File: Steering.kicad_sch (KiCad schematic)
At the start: 63 parts, among them J12 SERVO, J508 Conn_01x13, J509 Conn_01x03, J510 SWD, SW11 219-2MSTR, SW12 219-2MSTR, SW13 CVS-01TB, SW14 CVS-01TB, SW506 SW_Push, U13 STM32F401RETx, U14 MCP2515T-I/ST, U15 MCP2515T-I/ST, U16 SN65HVD230DR, U17 SN65HVD230DR, U18 INA180A1IDBVT, Y5 16 MHz, Y6 16 MHz

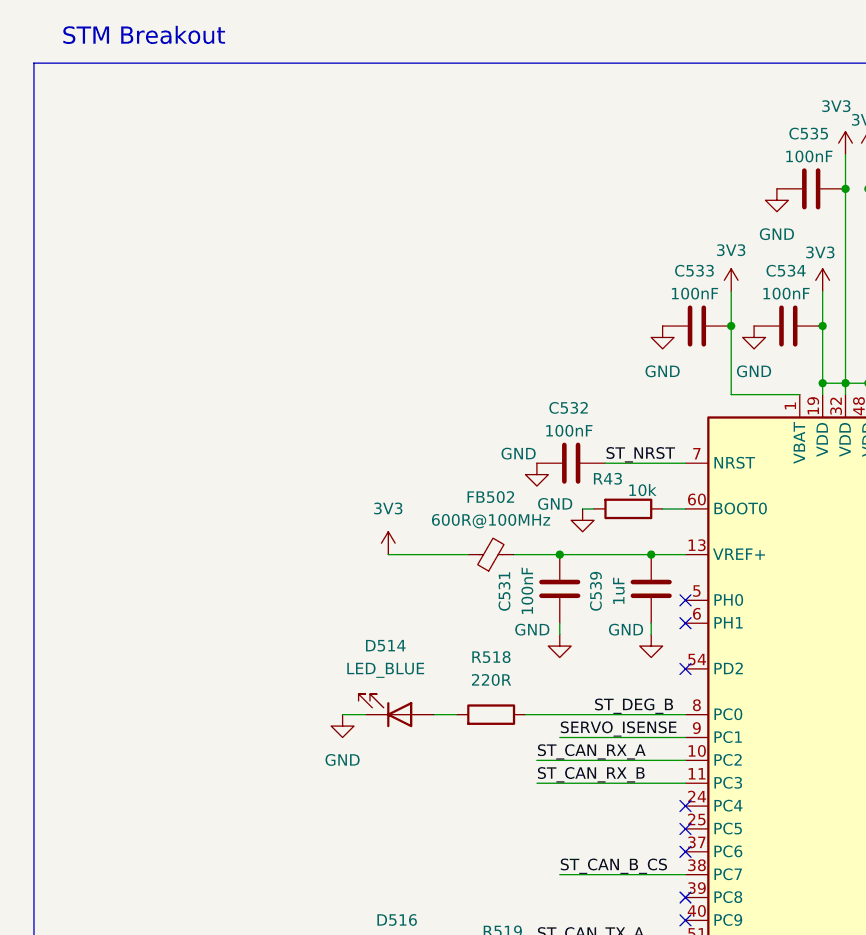
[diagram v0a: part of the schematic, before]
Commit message: Added 16MHz crystals to both STMs
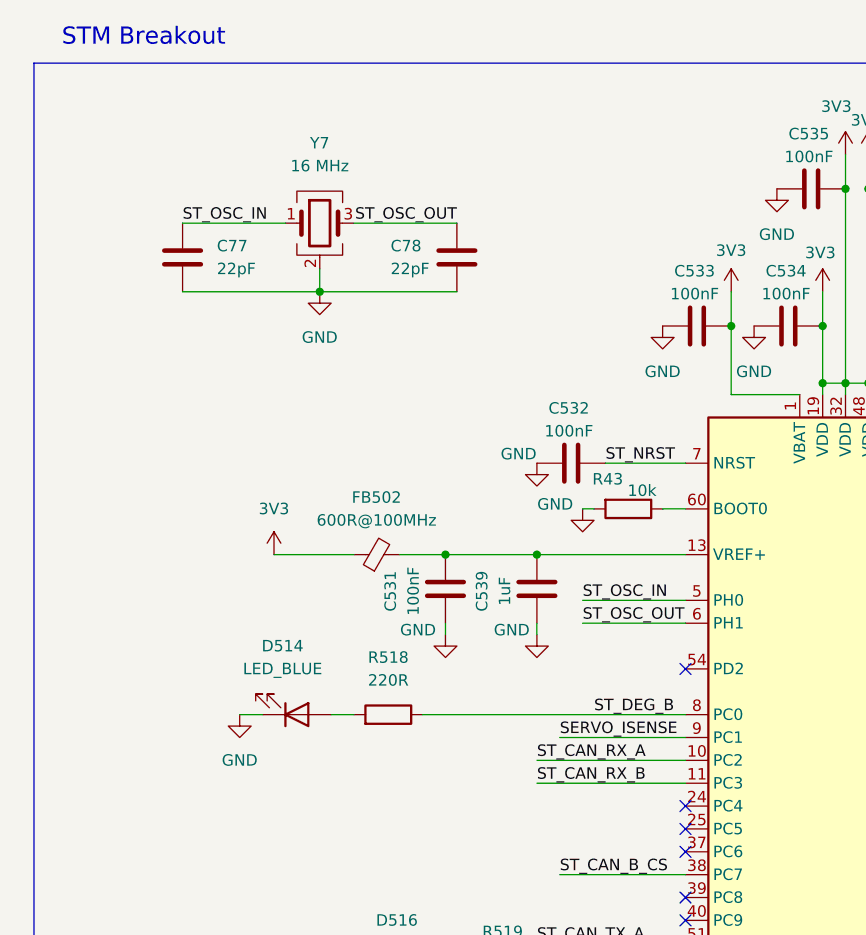
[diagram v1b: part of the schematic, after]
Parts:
- added C77, C78: 22pF, Capacitor_SMD:C_0603_1608Metric, symbol Device:C
- added Y7: 16 MHz, Crystal:Crystal_SMD_3225-4Pin_3.2x2.5mm, symbol Device:Crystal_GND24
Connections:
- net GND: now also C77.2, C78.2, Y7.2 (G), Y7.4 (G)
- net ST_OSC_IN: now reaches U13.5 (PH0)
- net ST_OSC_IN: now also C77.1, Y7.1
- net ST_OSC_OUT: now reaches U13.6 (PH1)
- net ST_OSC_OUT: now also C78.1, Y7.3
- no-connect marks 38 -> 36
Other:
- moved on the sheet: C531, C539, D514, FB502, R518

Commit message: Placement & Routing progress for ST and 8V buck
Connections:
- net SERVO_ISENSE: now also U13.14 (PA0); no longer U13.9 (PC1)
- net SERVO_PWM: now also J508.9 (Pin_9)
- net ST_CAN_RX_A: now also U13.37 (PC6); no longer U13.10 (PC2)
- net ST_CAN_RX_B: now also U13.36 (PB15); no longer U13.11 (PC3)
- net ST_CAN_TX_A: now also U13.35 (PB14); no longer U13.51 (PC10)
- net ST_CAN_TX_B: now also U13.34 (PB13); no longer U13.52 (PC11)
- net ST_DEG_A: now also R518.1, U13.8 (PC0); no longer R521.2, U13.61 (PB8)
- net ST_DEG_B: now also R521.1, U13.9 (PC1); no longer R518.1, U13.8 (PC0)
- net at D515.2 (A): now also R521.2; no longer R521.1
- net SRV: no longer names the net of U13.62 (PB9)
- net SRV: no longer J508.9 (Pin_9)
- no-connect marks 36 -> 37
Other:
- moved on the sheet: D517, R522

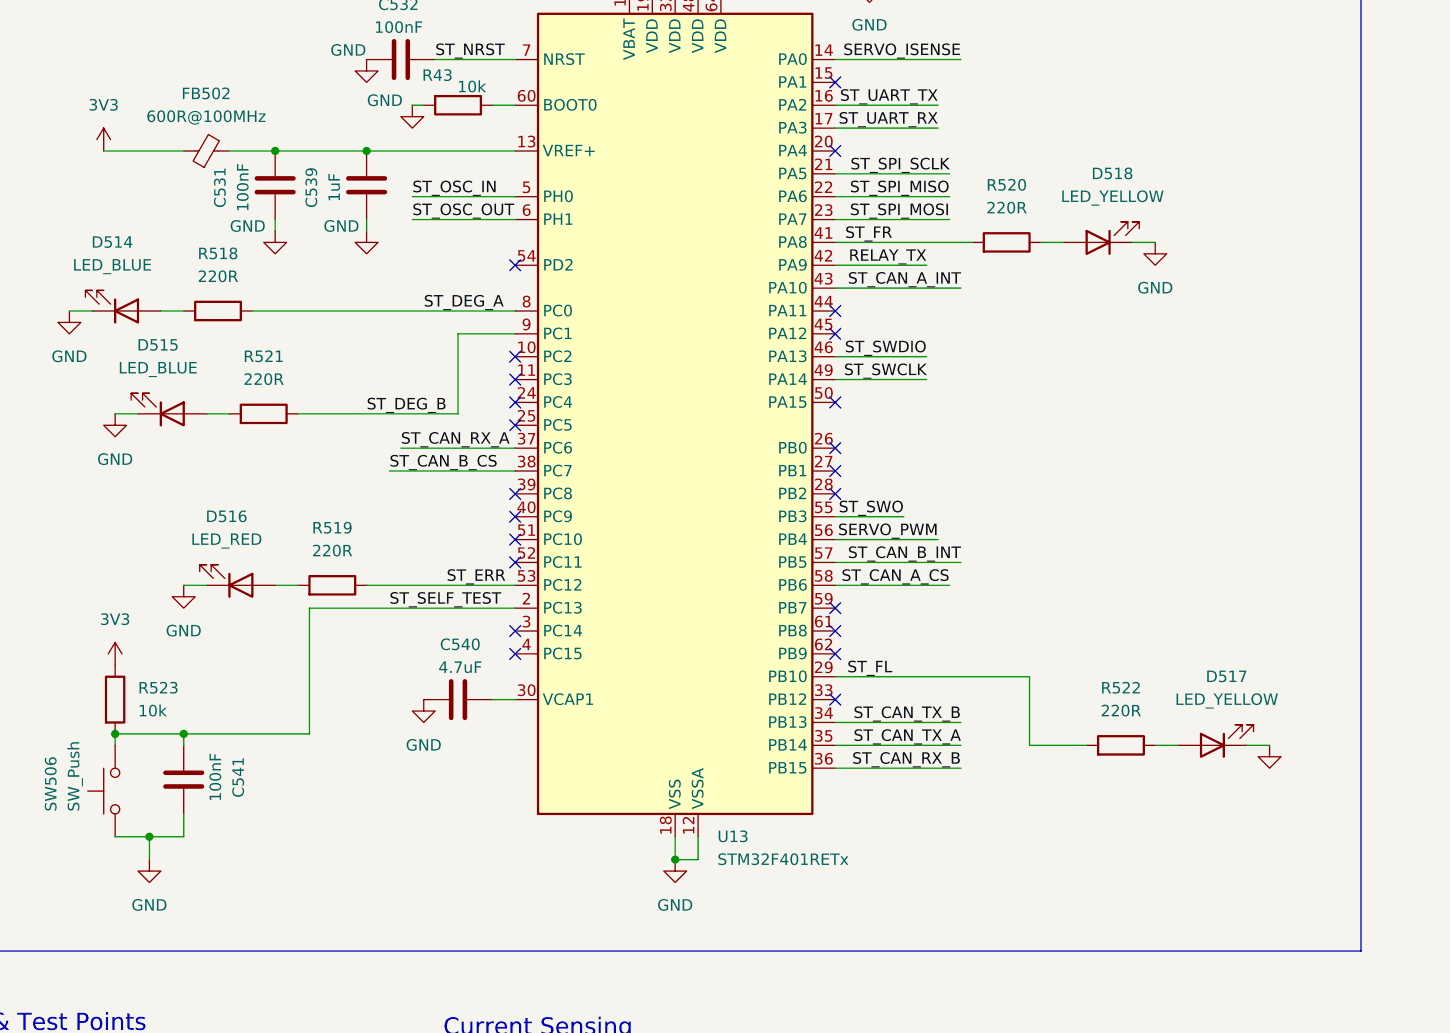
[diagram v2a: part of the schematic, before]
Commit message: Reduced congestion on steering
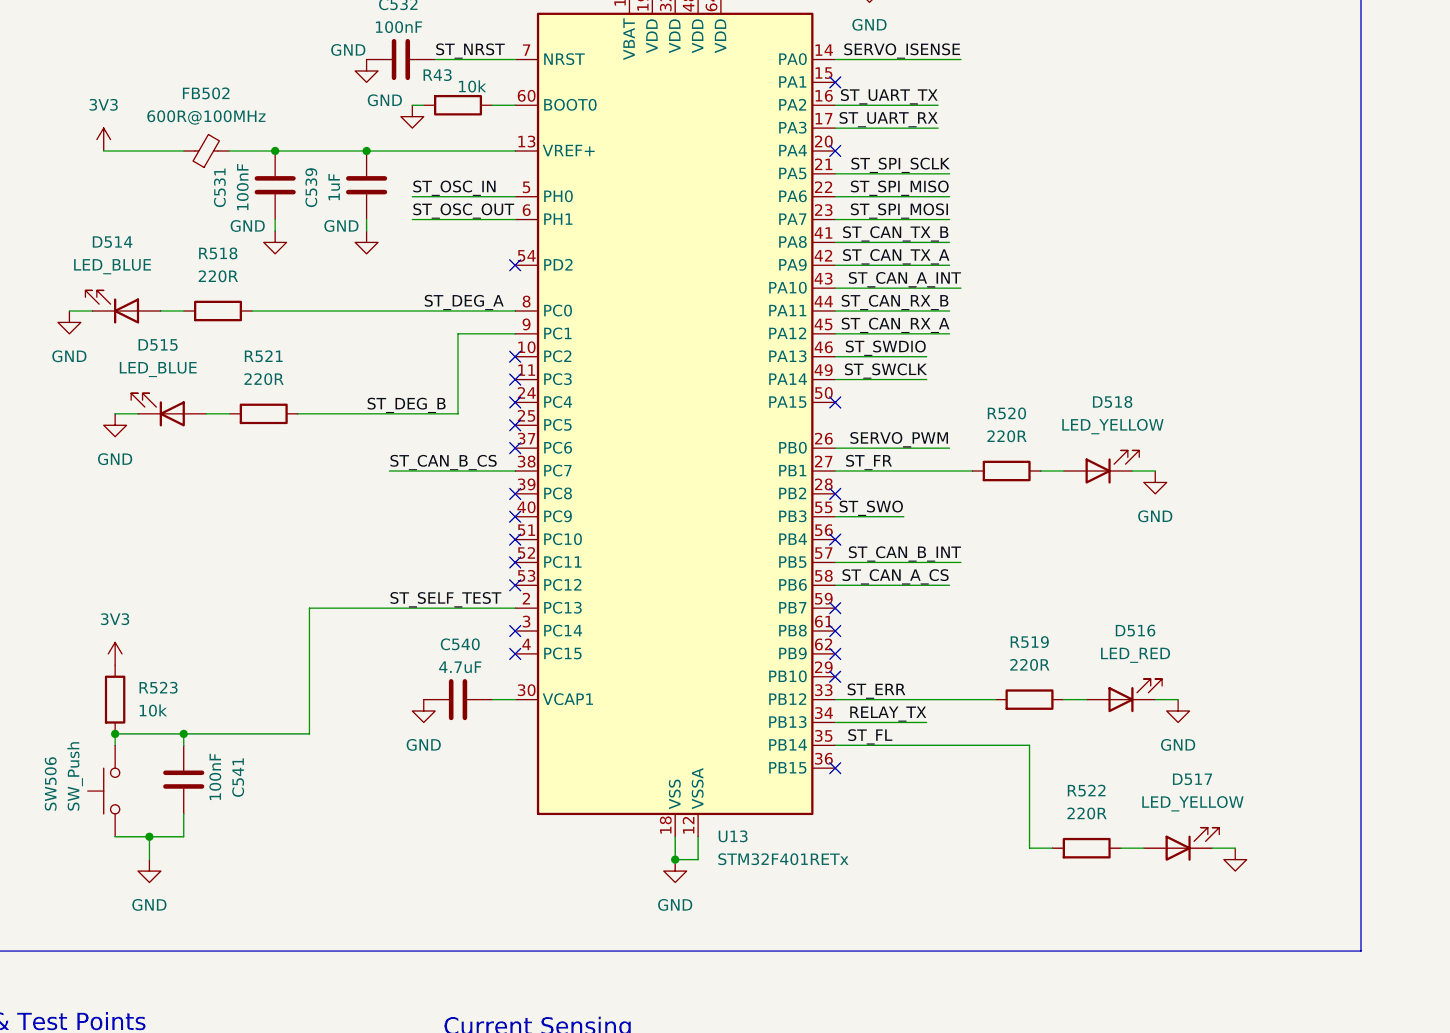
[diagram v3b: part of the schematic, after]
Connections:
- net RELAY_TX: now also U13.34 (PB13); no longer U13.42 (PA9)
- net SERVO_PWM: now also U13.26 (PB0); no longer U13.56 (PB4)
- net ST_CAN_RX_A: now also U13.45 (PA12); no longer U13.37 (PC6)
- net ST_CAN_RX_B: now also U13.44 (PA11); no longer U13.36 (PB15)
- net ST_CAN_TX_A: now also U13.42 (PA9); no longer U13.35 (PB14)
- net ST_CAN_TX_B: now also U13.41 (PA8); no longer U13.34 (PB13)
- net ST_ERR: now also R519.2, U13.33 (PB12); no longer R519.1, U13.53 (PC12)
- net ST_FL: now also U13.35 (PB14); no longer U13.29 (PB10)
- net ST_FR: now also U13.27 (PB1); no longer U13.41 (PA8)
- net at D516.2 (A): now also R519.1; no longer R519.2

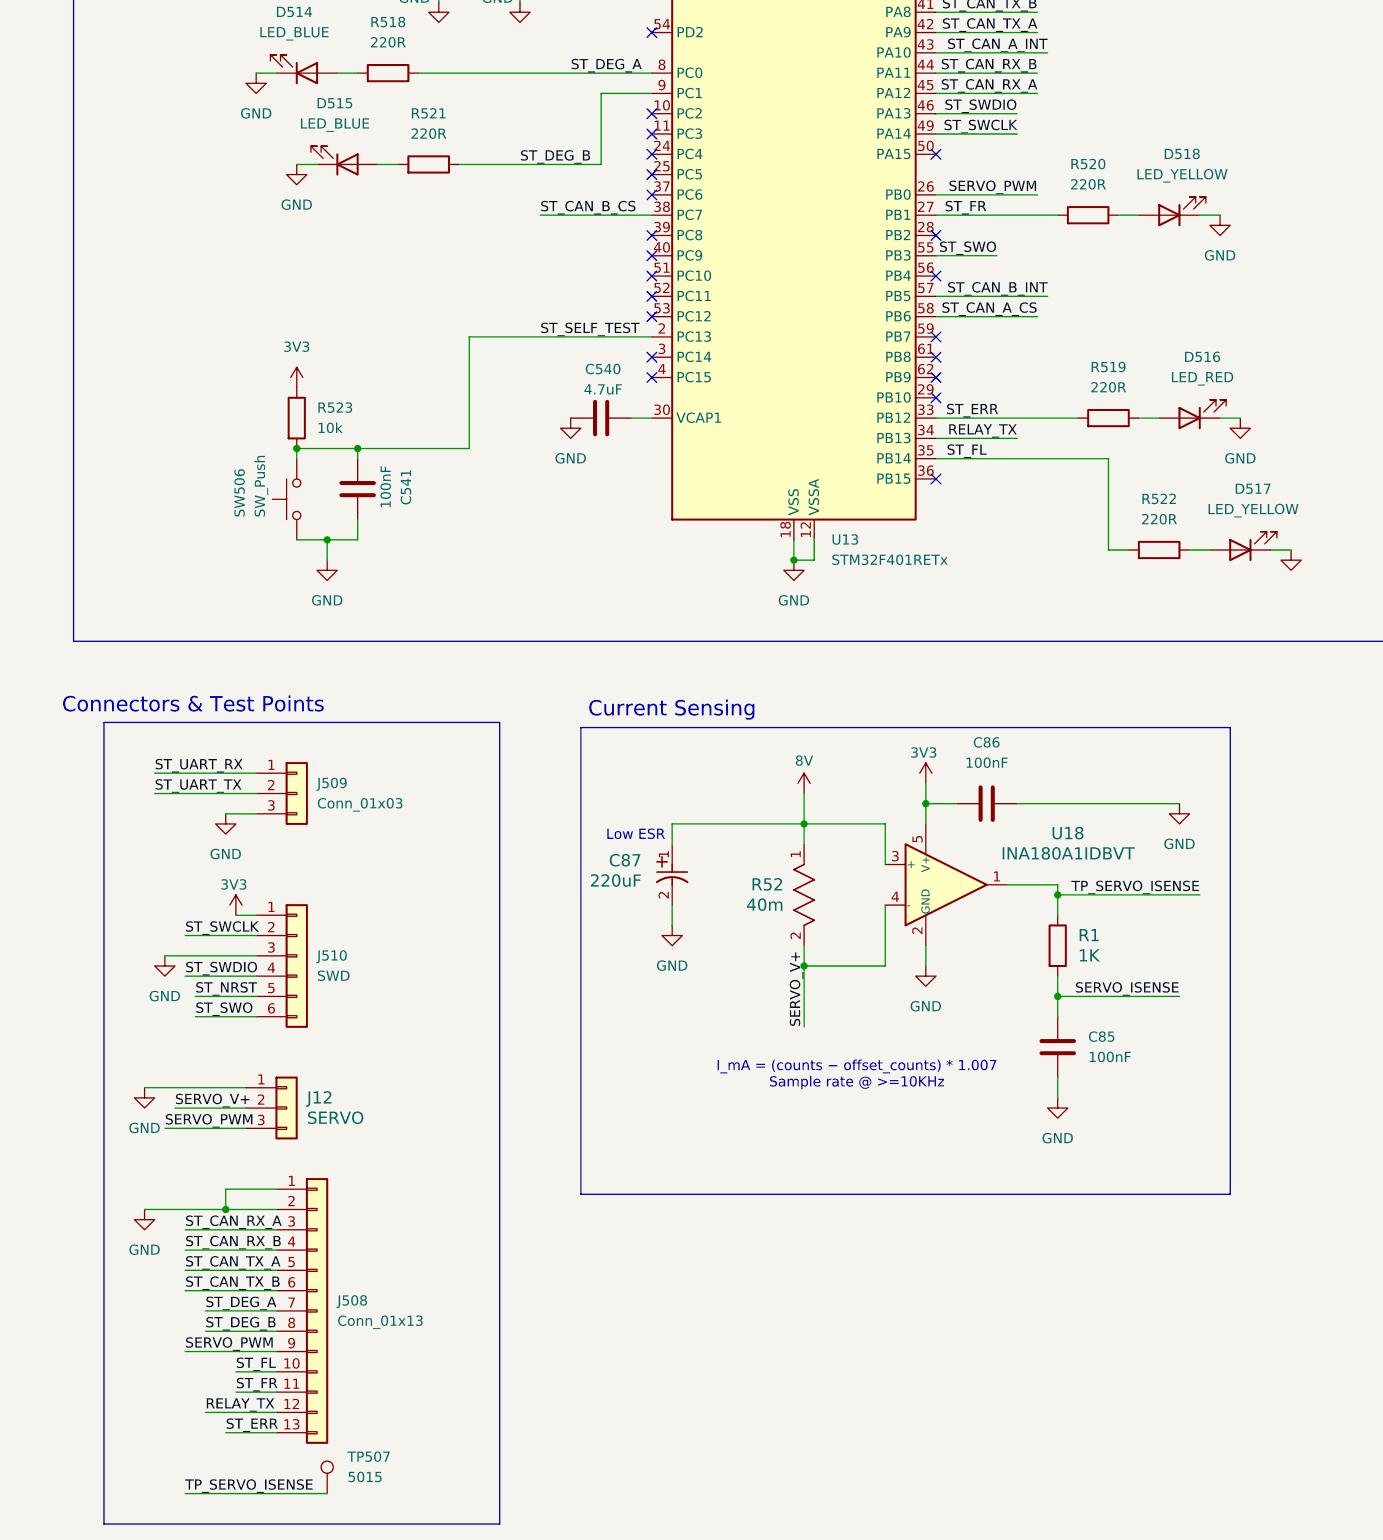
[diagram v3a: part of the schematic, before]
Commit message: Replaced ST pin header with test points
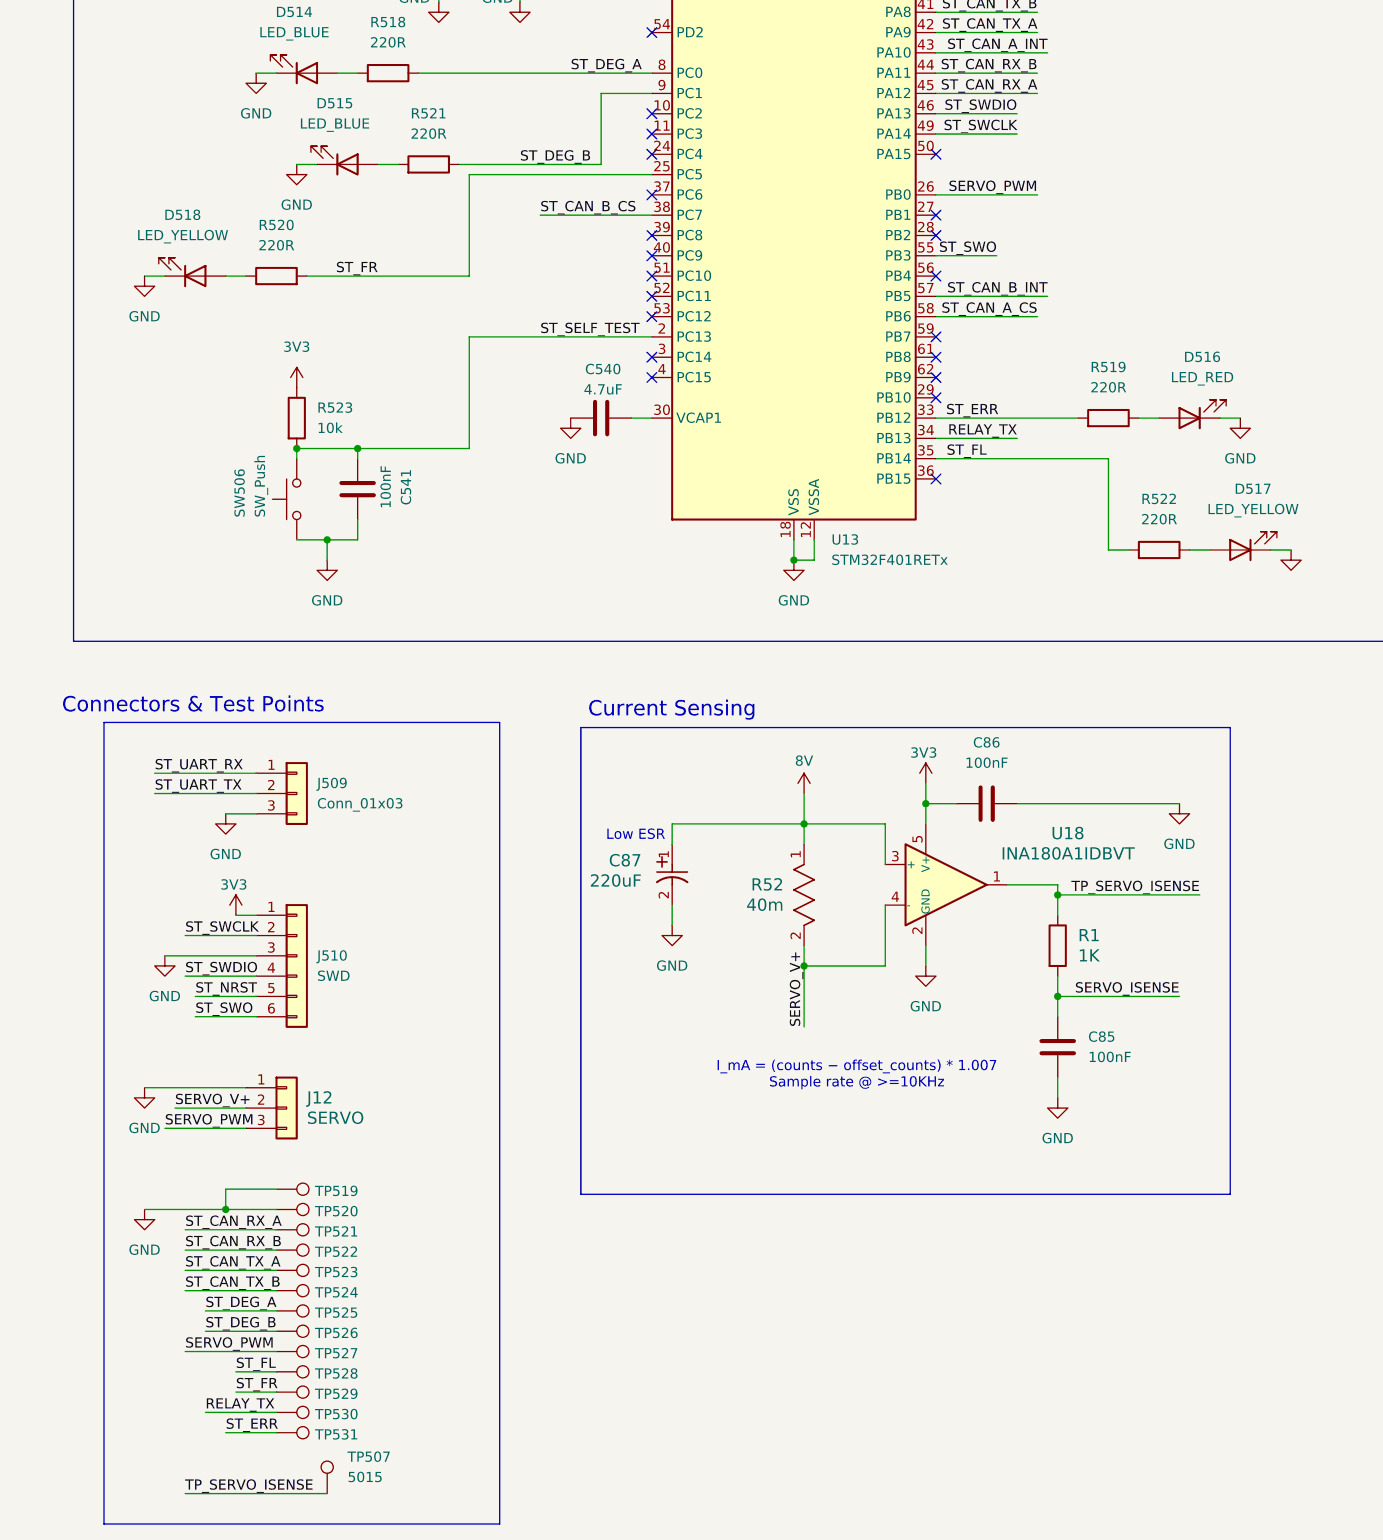
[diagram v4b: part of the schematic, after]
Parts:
- removed J508: Conn_01x13, Connector_PinHeader_2.54mm:PinHeader_1x13_P2.54mm_Vertical, symbol Connector_Generic:Conn_01x13
- added TP519, TP520, TP521, TP522, TP523, TP524, TP525, TP526, TP527, TP528, TP529, TP530, TP531: 5015, TestPoint:TestPoint_Keystone_5015_Micro_Mini, symbol Connector:TestPoint
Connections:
- net GND: now also TP519.1, TP520.1
- net RELAY_TX: now also TP530.1
- net SERVO_PWM: now also TP527.1
- net ST_CAN_RX_A: now also TP521.1
- net ST_CAN_RX_B: now also TP522.1
- net ST_CAN_TX_A: now also TP523.1
- net ST_CAN_TX_B: now also TP524.1
- net ST_DEG_A: now also TP525.1
- net ST_DEG_B: now also TP526.1
- net ST_ERR: now also TP531.1
- net ST_FL: now also TP528.1
- net ST_FR: now also U13.25 (PC5), TP529.1; no longer U13.27 (PB1)
